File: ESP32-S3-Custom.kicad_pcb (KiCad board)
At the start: 2 copper layers, 57.7 x 29 mm, 55 parts, among them J1 USB_C_Receptacle_USB2.0_16P, J2 USB_C_Receptacle_USB2.0_16P, J3 Conn_01x20, J4 Conn_01x20, Q1 SMD-TRANSISTORS-NPN-25V-500MW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, Q2 SMD-TRANSISTORS-NPN-25V-500MW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, SW1 SW_Push, SW2 SW_Push, U1 ESP32-S3-WROOM-1, U2 TLV75801PDRV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

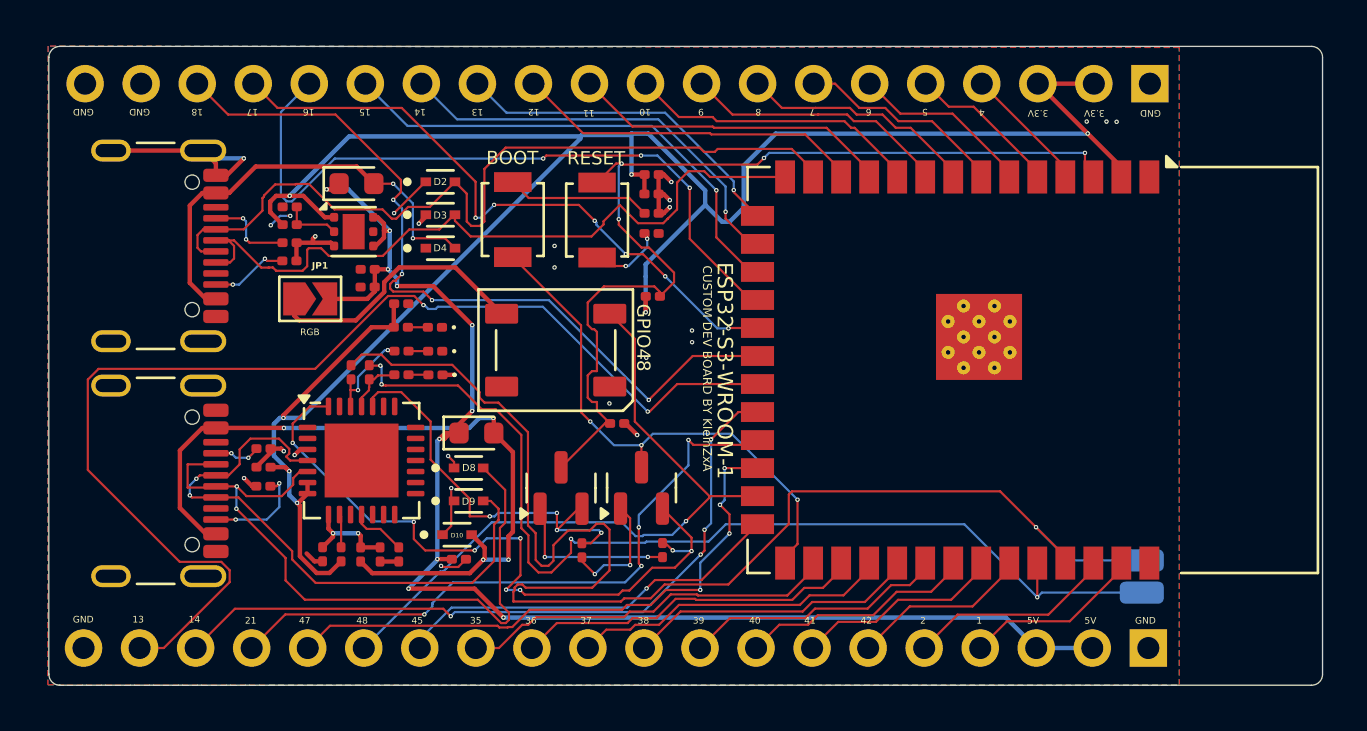
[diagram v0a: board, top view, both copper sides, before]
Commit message: Made to 4mm Via Diameter
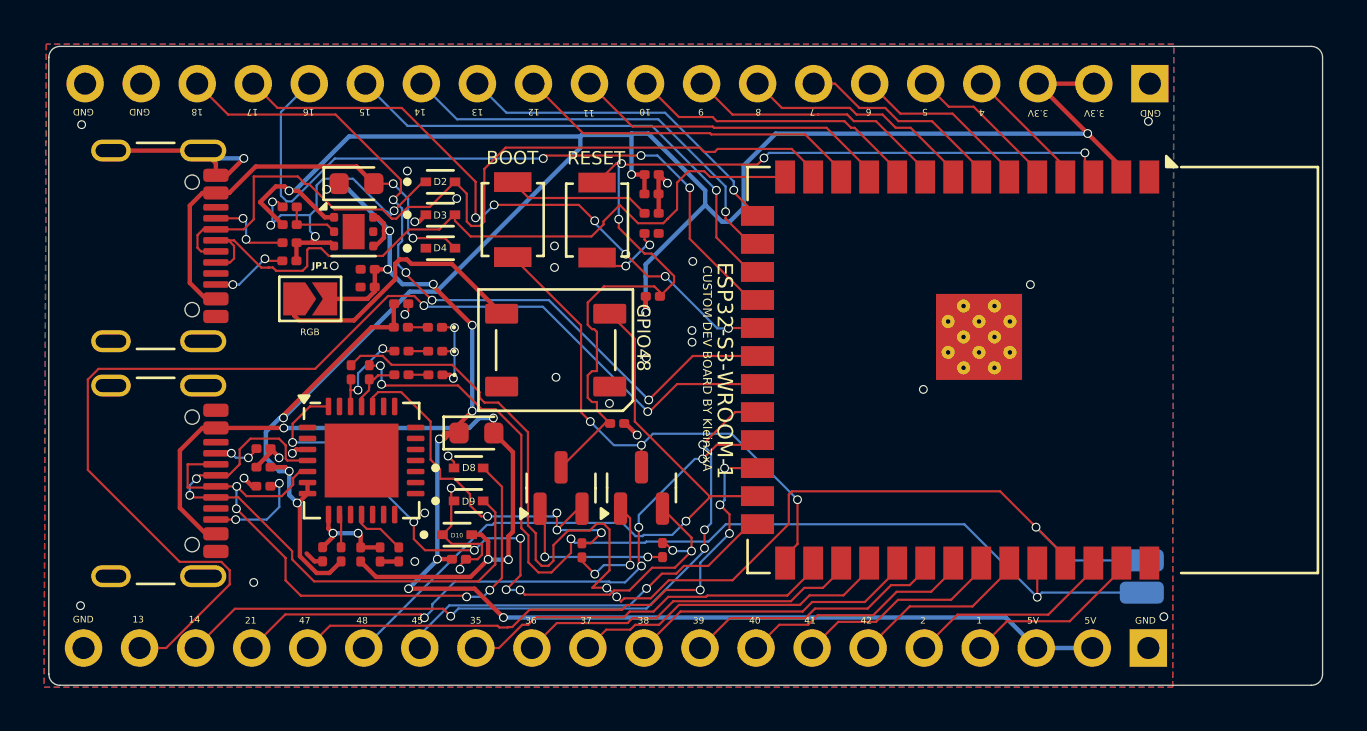
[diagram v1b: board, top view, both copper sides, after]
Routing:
- net GND: track 33.8 -> 48.4 mm, vias 27 -> 39
- net TX: track 62.6 -> 55.0 mm, vias 1 -> 3
- net Net-(U3-D-): track 32.4 -> 29.6 mm, vias 2 -> 4
- net VCC_3V3: track 103.3 -> 105.1 mm
- net GPIO_12: track 36.1 -> 35.0 mm
- net USB_D-: track 37.3 -> 38.4 mm
- net GPIO_21: track 29.3 -> 28.7 mm
